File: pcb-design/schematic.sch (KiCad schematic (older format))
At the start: 10 parts, among them J1 TempGauge, J2 FuelGauge, J3 SpeedInput_C2_P10-13, Q3 Q_NPN_BCE

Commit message: Schematic updates, learning KiCad a bit.
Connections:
- net labels added: FuelOutput, SpeedometerOutput, TemperatureOutput
- wire segments 6 -> 0
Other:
- moved on the sheet: J1, J2, J3, Q3, Q?, R1, R2, R3
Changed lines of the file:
@@
 L Device:Q_NPN_BCE Q?
 U 1 1 5D493CD9
-P 3600 5950
-F 0 "Q?" H 3791 5996 50  0000 L CNN
-F 1 "Q_NPN_BCE" H 3791 5905 50  0000 L CNN
-F 2 "" H 3800 6050 50  0001 C CNN
-F 3 "~" H 3600 5950 50  0001 C CNN
-	1    3600 5950
+P 9600 2700
+F 0 "Q?" H 9791 2746 50  0000 L CNN
+F 1 "Q_NPN_BCE" H 9791 2655 50  0000 L CNN
+F 2 "" H 9800 2800 50  0001 C CNN
+F 3 "~" H 9600 2700 50  0001 C CNN
+	1    9600 2700
 	1    0    0    -1
 $EndComp
@@
 L Device:R_Small_US R2
 U 1 1 5D49723D
-P 3300 5950
-F 0 "R2" V 3095 5950 50  0000 C CNN
-F 1 "220" V 3186 5950 50  0000 C CNN
-F 2 "" H 3300 5950 50  0001 C CNN
-F 3 "~" H 3300 5950 50  0001 C CNN
-	1    3300 5950
+P 9300 2700
+F 0 "R2" V 9095 2700 50  0000 C CNN
+F 1 "220" V 9186 2700 50  0000 C CNN
+F 2 "" H 9300 2700 50  0001 C CNN
+F 3 "~" H 9300 2700 50  0001 C CNN
+	1    9300 2700
 	0    1    1    0
 $EndComp
-Wire Wire Line
-	3050 3300 3200 3300
 $Comp
 L Device:Q_NPN_BCE Q?
 U 1 1 5D49F77C
-P 3600 5150
-F 0 "Q?" H 3791 5196 50  0000 L CNN
-F 1 "Q_NPN_BCE" H 3791 5105 50  0000 L CNN
-F 2 "" H 3800 5250 50  0001 C CNN
-F 3 "~" H 3600 5150 50  0001 C CNN
-	1    3600 5150
+P 9600 1800
+F 0 "Q?" H 9791 1846 50  0000 L CNN
+F 1 "Q_NPN_BCE" H 9791 1755 50  0000 L CNN
+F 2 "" H 9800 1900 50  0001 C CNN
+F 3 "~" H 9600 1800 50  0001 C CNN
+	1    9600 1800
 	1    0    0    -1
 $EndComp
@@
 L Device:R_Small_US R1
 U 1 1 5D49F782
-P 3300 5150
-F 0 "R1" V 3095 5150 50  0000 C CNN
-F 1 "470" V 3186 5150 50  0000 C CNN
-F 2 "" H 3300 5150 50  0001 C CNN
-F 3 "~" H 3300 5150 50  0001 C CNN
-	1    3300 5150
+P 9300 1800
+F 0 "R1" V 9095 1800 50  0000 C CNN
+F 1 "470" V 9186 1800 50  0000 C CNN
+F 2 "" H 9300 1800 50  0001 C CNN
+F 3 "~" H 9300 1800 50  0001 C CNN
+	1    9300 1800
 	0    1    1    0
 $EndComp
-Wire Wire Line
-	3200 5150 3200 3300
-Wire Wire Line
-	3200 5950 3150 5950
-Wire Wire Line
-	3150 3400 3050 3400
 $Comp
 L Connector:Conn_01x01_Male J1
 U 1 1 5D4A2526
-P 3900 4950
-F 0 "J1" H 3872 4882 50  0000 R CNN
-F 1 "TempGauge" H 3872 4973 50  0000 R CNN
-F 2 "" H 3900 4950 50  0001 C CNN
-F 3 "~" H 3900 4950 50  0001 C CNN
-	1    3900 4950
+P 9900 1600
+F 0 "J1" H 9872 1532 50  0000 R CNN
+F 1 "TempGauge" H 9872 1623 50  0000 R CNN
+F 2 "" H 9900 1600 50  0001 C CNN
+F 3 "~" H 9900 1600 50  0001 C CNN
+	1    9900 1600
 	-1   0    0    1
 $EndComp
@@
 L Connector:Conn_01x01_Male J2
 U 1 1 5D4A3714
-P 3900 5750
-F 0 "J2" H 3872 5682 50  0000 R CNN
-F 1 "FuelGauge" H 3872 5773 50  0000 R CNN
-F 2 "" H 3900 5750 50  0001 C CNN
-F 3 "~" H 3900 5750 50  0001 C CNN
-	1    3900 5750
+P 9900 2500
+F 0 "J2" H 9872 2432 50  0000 R CNN
+F 1 "FuelGauge" H 9872 2523 50  0000 R CNN
+F 2 "" H 9900 2500 50  0001 C CNN
+F 3 "~" H 9900 2500 50  0001 C CNN
+	1    9900 2500
 	-1   0    0    1
 $EndComp
@@
 L power:GND #PWR?
 U 1 1 5D4A41B3
-P 3700 5350
-F 0 "#PWR?" H 3700 5100 50  0001 C CNN
-F 1 "GND" H 3705 5177 50  0000 C CNN
-F 2 "" H 3700 5350 50  0001 C CNN
-F 3 "" H 3700 5350 50  0001 C CNN
-	1    3700 5350
+P 9700 2000
+F 0 "#PWR?" H 9700 1750 50  0001 C CNN
+F 1 "GND" H 9705 1827 50  0000 C CNN
+F 2 "" H 9700 2000 50  0001 C CNN
+F 3 "" H 9700 2000 50  0001 C CNN
+	1    9700 2000
 	1    0    0    -1
 $EndComp
@@
 L power:GND #PWR?
 U 1 1 5D4A53EC
-P 3700 6150
-F 0 "#PWR?" H 3700 5900 50  0001 C CNN
-F 1 "GND" H 3705 5977 50  0000 C CNN
-F 2 "" H 3700 6150 50  0001 C CNN
-F 3 "" H 3700 6150 50  0001 C CNN
-	1    3700 6150
+P 9700 2900
+F 0 "#PWR?" H 9700 2650 50  0001 C CNN
+F 1 "GND" H 9705 2727 50  0000 C CNN
+F 2 "" H 9700 2900 50  0001 C CNN
+F 3 "" H 9700 2900 50  0001 C CNN
+	1    9700 2900
 	1    0    0    -1
 $EndComp
-Wire Wire Line
-	3150 3400 3150 5950
 $Comp
 L Device:Q_NPN_BCE Q3
 U 1 1 5DD62680
-P 5800 3200
-F 0 "Q3" H 5991 3246 50  0000 L CNN
-F 1 "Q_NPN_BCE" H 5991 3155 50  0000 L CNN
-F 2 "" H 6000 3300 50  0001 C CNN
-F 3 "~" H 5800 3200 50  0001 C CNN
-	1    5800 3200
+P 9600 1050
+F 0 "Q3" H 9791 1096 50  0000 L CNN
+F 1 "Q_NPN_BCE" H 9791 1005 50  0000 L CNN
+F 2 "" H 9800 1150 50  0001 C CNN
+F 3 "~" H 9600 1050 50  0001 C CNN
+	1    9600 1050
 	1    0    0    -1
 $EndComp
@@
 L Device:R_Small_US R3
 U 1 1 5DD62687
-P 5500 3200
-F 0 "R3" V 5295 3200 50  0000 C CNN
-F 1 "470" V 5386 3200 50  0000 C CNN
-F 2 "" H 5500 3200 50  0001 C CNN
-F 3 "~" H 5500 3200 50  0001 C CNN
-	1    5500 3200
+P 9300 1050
+F 0 "R3" V 9095 1050 50  0000 C CNN
+F 1 "470" V 9186 1050 50  0000 C CNN
+F 2 "" H 9300 1050 50  0001 C CNN
+F 3 "~" H 9300 1050 50  0001 C CNN
+	1    9300 1050
 	0    1    1    0
 $EndComp
@@
 L Connector:Conn_01x01_Male J3
 U 1 1 5DD6268E
-P 6100 3000
-F 0 "J3" H 6072 2932 50  0000 R CNN
-F 1 "SpeedInput_C2_P10-13" H 6072 3023 50  0000 R CNN
-F 2 "" H 6100 3000 50  0001 C CNN
-F 3 "~" H 6100 3000 50  0001 C CNN
-	1    6100 3000
+P 9900 850
+F 0 "J3" H 9872 782 50  0000 R CNN
+F 1 "SpeedInput_C2_P10-13" H 9872 873 50  0000 R CNN
+F 2 "" H 9900 850 50  0001 C CNN
+F 3 "~" H 9900 850 50  0001 C CNN
+	1    9900 850
 	-1   0    0    1
 $EndComp
@@
 L power:GND #PWR?
 U 1 1 5DD62695
-P 5900 3400
-F 0 "#PWR?" H 5900 3150 50  0001 C CNN
-F 1 "GND" H 5905 3227 50  0000 C CNN
-F 2 "" H 5900 3400 50  0001 C CNN
-F 3 "" H 5900 3400 50  0001 C CNN
-	1    5900 3400
+P 9700 1250
+F 0 "#PWR?" H 9700 1000 50  0001 C CNN
+F 1 "GND" H 9705 1077 50  0000 C CNN
+F 2 "" H 9700 1250 50  0001 C CNN
+F 3 "" H 9700 1250 50  0001 C CNN
+	1    9700 1250
 	1    0    0    -1
 $EndComp
-Wire Wire Line
-	3050 3200 5400 3200
+Text GLabel 9200 1050 0    50   Input ~ 0
+SpeedometerOutput
+Text GLabel 9200 1800 0    50   Input ~ 0
+TemperatureOutput
+Text GLabel 9200 2700 0    50   Input ~ 0
+FuelOutput
 $EndSCHEMATC

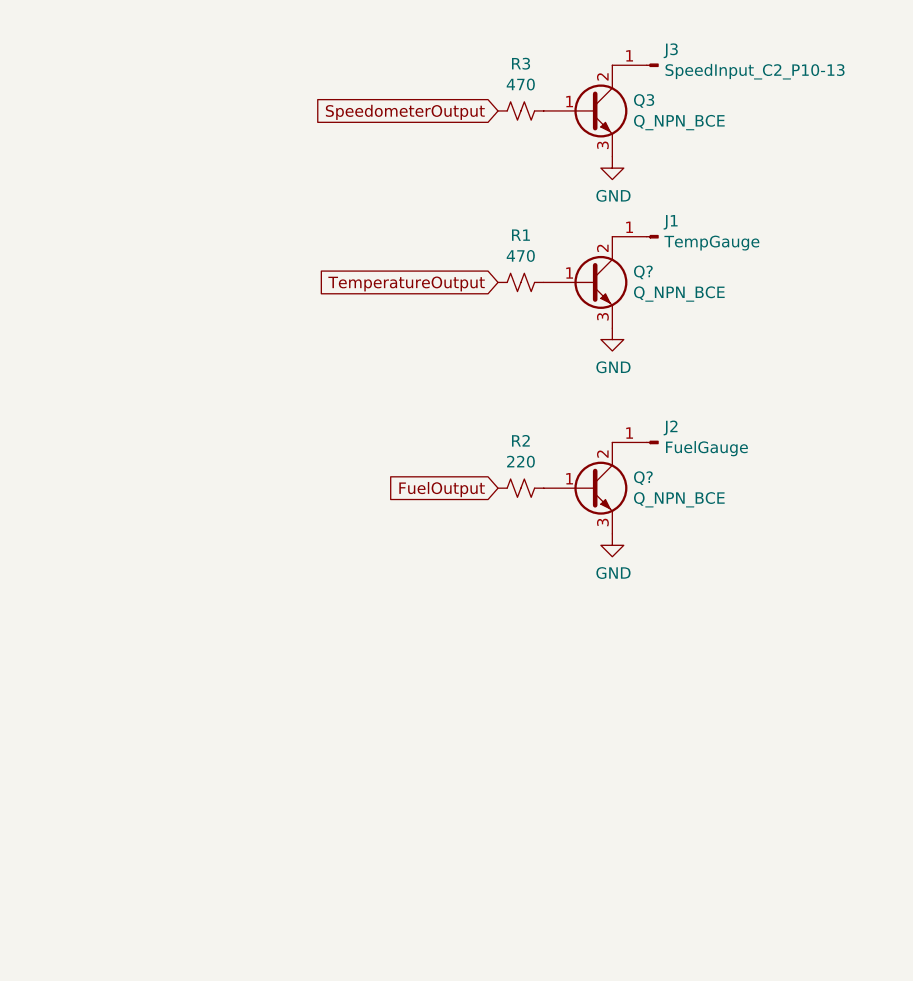
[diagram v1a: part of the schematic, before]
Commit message: Added Tachometer circuit to schematic
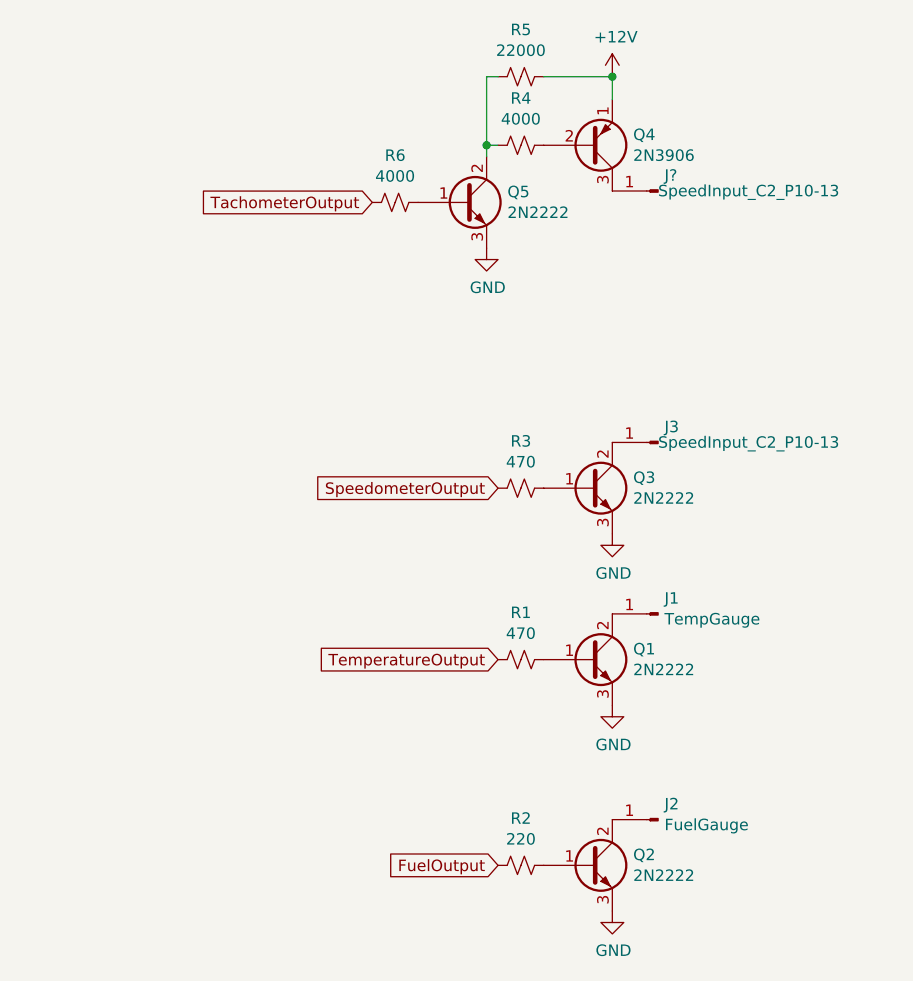
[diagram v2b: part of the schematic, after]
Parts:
- added J?: SpeedInput_C2_P10-13, symbol Connector:Conn_01x01_Male
- added Q4: 2N3906, Package_TO_SOT_THT:TO-92_Inline, symbol Transistor_BJT:2N3906
- added Q5: 2N2222, symbol Device:Q_NPN_BCE
- added R4, R6: 4000, symbol Device:R_Small_US
- added R5: 22000, symbol Device:R_Small_US
- Q1, Q2: renamed from Q?; value Q_NPN_BCE -> 2N2222
- Q3: value Q_NPN_BCE -> 2N2222
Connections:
- net labels added: +12V, TachometerOutput
- wire segments 0 -> 6
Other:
- moved on the sheet: J1, J2, J3, Q1, Q2, Q3, R1, R2, R3
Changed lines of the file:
@@
 $EndComp
 $Comp
-L Device:Q_NPN_BCE Q?
+L Device:Q_NPN_BCE Q2
 U 1 1 5D493CD9
+P 9600 4350
+F 0 "Q2" H 9791 4396 50  0000 L CNN
+F 1 "2N2222" H 9791 4305 50  0000 L CNN
+F 2 "" H 9800 4450 50  0001 C CNN
+F 3 "~" H 9600 4350 50  0001 C CNN
+	1    9600 4350
+	1    0    0    -1
+$EndComp
+$Comp
+L Device:R_Small_US R2
+U 1 1 5D49723D
+P 9300 4350
+F 0 "R2" V 9095 4350 50  0000 C CNN
+F 1 "220" V 9186 4350 50  0000 C CNN
+F 2 "" H 9300 4350 50  0001 C CNN
+F 3 "~" H 9300 4350 50  0001 C CNN
+	1    9300 4350
+	0    1    1    0
+$EndComp
+$Comp
+L Device:Q_NPN_BCE Q1
+U 1 1 5D49F77C
+P 9600 3450
+F 0 "Q1" H 9791 3496 50  0000 L CNN
+F 1 "2N2222" H 9791 3405 50  0000 L CNN
+F 2 "" H 9800 3550 50  0001 C CNN
+F 3 "~" H 9600 3450 50  0001 C CNN
+	1    9600 3450
+	1    0    0    -1
+$EndComp
+$Comp
+L Device:R_Small_US R1
+U 1 1 5D49F782
+P 9300 3450
+F 0 "R1" V 9095 3450 50  0000 C CNN
+F 1 "470" V 9186 3450 50  0000 C CNN
+F 2 "" H 9300 3450 50  0001 C CNN
+F 3 "~" H 9300 3450 50  0001 C CNN
+	1    9300 3450
+	0    1    1    0
+$EndComp
+$Comp
+L Connector:Conn_01x01_Male J1
+U 1 1 5D4A2526
+P 9900 3250
+F 0 "J1" H 9872 3182 50  0000 R CNN
+F 1 "TempGauge" H 9872 3273 50  0000 R CNN
+F 2 "" H 9900 3250 50  0001 C CNN
+F 3 "~" H 9900 3250 50  0001 C CNN
+	1    9900 3250
+	-1   0    0    1
+$EndComp
+$Comp
+L Connector:Conn_01x01_Male J2
+U 1 1 5D4A3714
+P 9900 4150
+F 0 "J2" H 9872 4082 50  0000 R CNN
+F 1 "FuelGauge" H 9872 4173 50  0000 R CNN
+F 2 "" H 9900 4150 50  0001 C CNN
+F 3 "~" H 9900 4150 50  0001 C CNN
+	1    9900 4150
+	-1   0    0    1
+$EndComp
+$Comp
+L power:GND #PWR?
+U 1 1 5D4A41B3
+P 9700 3650
+F 0 "#PWR?" H 9700 3400 50  0001 C CNN
+F 1 "GND" H 9705 3477 50  0000 C CNN
+F 2 "" H 9700 3650 50  0001 C CNN
+F 3 "" H 9700 3650 50  0001 C CNN
+	1    9700 3650
+	1    0    0    -1
+$EndComp
+$Comp
+L power:GND #PWR?
+U 1 1 5D4A53EC
+P 9700 4550
+F 0 "#PWR?" H 9700 4300 50  0001 C CNN
+F 1 "GND" H 9705 4377 50  0000 C CNN
+F 2 "" H 9700 4550 50  0001 C CNN
+F 3 "" H 9700 4550 50  0001 C CNN
+	1    9700 4550
+	1    0    0    -1
+$EndComp
+$Comp
+L Device:Q_NPN_BCE Q3
+U 1 1 5DD62680
 P 9600 2700
-F 0 "Q?" H 9791 2746 50  0000 L CNN
-F 1 "Q_NPN_BCE" H 9791 2655 50  0000 L CNN
+F 0 "Q3" H 9791 2746 50  0000 L CNN
+F 1 "2N2222" H 9791 2655 50  0000 L CNN
 F 2 "" H 9800 2800 50  0001 C CNN
 F 3 "~" H 9600 2700 50  0001 C CNN
@@
 $EndComp
 $Comp
-L Device:R_Small_US R2
-U 1 1 5D49723D
+L Device:R_Small_US R3
+U 1 1 5DD62687
 P 9300 2700
-F 0 "R2" V 9095 2700 50  0000 C CNN
-F 1 "220" V 9186 2700 50  0000 C CNN
+F 0 "R3" V 9095 2700 50  0000 C CNN
+F 1 "470" V 9186 2700 50  0000 C CNN
 F 2 "" H 9300 2700 50  0001 C CNN
 F 3 "~" H 9300 2700 50  0001 C CNN
@@
 $EndComp
 $Comp
-L Device:Q_NPN_BCE Q?
-U 1 1 5D49F77C
-P 9600 1800
-F 0 "Q?" H 9791 1846 50  0000 L CNN
-F 1 "Q_NPN_BCE" H 9791 1755 50  0000 L CNN
-F 2 "" H 9800 1900 50  0001 C CNN
-F 3 "~" H 9600 1800 50  0001 C CNN
-	1    9600 1800
-	1    0    0    -1
-$EndComp
-$Comp
-L Device:R_Small_US R1
-U 1 1 5D49F782
-P 9300 1800
-F 0 "R1" V 9095 1800 50  0000 C CNN
-F 1 "470" V 9186 1800 50  0000 C CNN
-F 2 "" H 9300 1800 50  0001 C CNN
-F 3 "~" H 9300 1800 50  0001 C CNN
-	1    9300 1800
-	0    1    1    0
-$EndComp
-$Comp
-L Connector:Conn_01x01_Male J1
-U 1 1 5D4A2526
-P 9900 1600
-F 0 "J1" H 9872 1532 50  0000 R CNN
-F 1 "TempGauge" H 9872 1623 50  0000 R CNN
-F 2 "" H 9900 1600 50  0001 C CNN
-F 3 "~" H 9900 1600 50  0001 C CNN
-	1    9900 1600
-	-1   0    0    1
-$EndComp
-$Comp
-L Connector:Conn_01x01_Male J2
-U 1 1 5D4A3714
+L Connector:Conn_01x01_Male J3
+U 1 1 5DD6268E
 P 9900 2500
-F 0 "J2" H 9872 2432 50  0000 R CNN
-F 1 "FuelGauge" H 9872 2523 50  0000 R CNN
+F 0 "J3" H 9872 2432 50  0000 R CNN
+F 1 "SpeedInput_C2_P10-13" H 9900 2500 50  0000 R CNN
 F 2 "" H 9900 2500 50  0001 C CNN
 F 3 "~" H 9900 2500 50  0001 C CNN
@@
 $Comp
 L power:GND #PWR?
-U 1 1 5D4A41B3
-P 9700 2000
-F 0 "#PWR?" H 9700 1750 50  0001 C CNN
-F 1 "GND" H 9705 1827 50  0000 C CNN
-F 2 "" H 9700 2000 50  0001 C CNN
-F 3 "" H 9700 2000 50  0001 C CNN
-	1    9700 2000
-	1    0    0    -1
-$EndComp
-$Comp
-L power:GND #PWR?
-U 1 1 5D4A53EC
+U 1 1 5DD62695
 P 9700 2900
 F 0 "#PWR?" H 9700 2650 50  0001 C CNN
@@
 	1    0    0    -1
 $EndComp
-$Comp
-L Device:Q_NPN_BCE Q3
-U 1 1 5DD62680
-P 9600 1050
-F 0 "Q3" H 9791 1096 50  0000 L CNN
-F 1 "Q_NPN_BCE" H 9791 1005 50  0000 L CNN
-F 2 "" H 9800 1150 50  0001 C CNN
-F 3 "~" H 9600 1050 50  0001 C CNN
-	1    9600 1050
-	1    0    0    -1
-$EndComp
-$Comp
-L Device:R_Small_US R3
-U 1 1 5DD62687
-P 9300 1050
-F 0 "R3" V 9095 1050 50  0000 C CNN
-F 1 "470" V 9186 1050 50  0000 C CNN
-F 2 "" H 9300 1050 50  0001 C CNN
-F 3 "~" H 9300 1050 50  0001 C CNN
-	1    9300 1050
-	0    1    1    0
-$EndComp
-$Comp
-L Connector:Conn_01x01_Male J3
-U 1 1 5DD6268E
-P 9900 850
-F 0 "J3" H 9872 782 50  0000 R CNN
-F 1 "SpeedInput_C2_P10-13" H 9872 873 50  0000 R CNN
-F 2 "" H 9900 850 50  0001 C CNN
-F 3 "~" H 9900 850 50  0001 C CNN
-	1    9900 850
-	-1   0    0    1
-$EndComp
-$Comp
-L power:GND #PWR?
-U 1 1 5DD62695
-P 9700 1250
-F 0 "#PWR?" H 9700 1000 50  0001 C CNN
-F 1 "GND" H 9705 1077 50  0000 C CNN
-F 2 "" H 9700 1250 50  0001 C CNN
-F 3 "" H 9700 1250 50  0001 C CNN
-	1    9700 1250
-	1    0    0    -1
-$EndComp
-Text GLabel 9200 1050 0    50   Input ~ 0
+Text GLabel 9200 2700 0    50   Input ~ 0
 SpeedometerOutput
-Text GLabel 9200 1800 0    50   Input ~ 0
+Text GLabel 9200 3450 0    50   Input ~ 0
 TemperatureOutput
-Text GLabel 9200 2700 0    50   Input ~ 0
+Text GLabel 9200 4350 0    50   Input ~ 0
 FuelOutput
+$Comp
+L Transistor_BJT:2N3906 Q4
+U 1 1 5DDF4E90
+P 9600 1200
+F 0 "Q4" H 9791 1154 50  0000 L CNN
+F 1 "2N3906" H 9791 1245 50  0000 L CNN
+F 2 "Package_TO_SOT_THT:TO-92_Inline" H 9800 1125 50  0001 L CIN
+F 3 "https://www.fairchildsemi.com/datasheets/2N/2N3906.pdf" H 9600 1200 50  0001 L CNN
+	1    9600 1200
+	1    0    0    1
+$EndComp
+$Comp
+L Device:R_Small_US R4
+U 1 1 5DDF52DA
+P 9300 1200
+F 0 "R4" V 9095 1200 50  0000 C CNN
+F 1 "4000" V 9186 1200 50  0000 C CNN
+F 2 "" H 9300 1200 50  0001 C CNN
+F 3 "~" H 9300 1200 50  0001 C CNN
+	1    9300 1200
+	0    1    1    0
+$EndComp
+$Comp
+L Device:R_Small_US R5
+U 1 1 5DDF54A7
+P 9300 900
+F 0 "R5" V 9095 900 50  0000 C CNN
+F 1 "22000" V 9186 900 50  0000 C CNN
+F 2 "" H 9300 900 50  0001 C CNN
+F 3 "~" H 9300 900 50  0001 C CNN
+	1    9300 900
+	0    1    1    0
+$EndComp
+Wire Wire Line
+	9200 1200 9150 1200
+Wire Wire Line
+	9150 1200 9150 1250
+Wire Wire Line
+	9700 1000 9700 900
+Wire Wire Line
+	9700 900  9400 900
+Wire Wire Line
+	9200 900  9150 900
+Wire Wire Line
+	9150 900  9150 1200
+Connection ~ 9150 1200
+$Comp
+L Device:R_Small_US R6
+U 1 1 5DDF56FD
+P 8750 1450
+F 0 "R6" V 8545 1450 50  0000 C CNN
+F 1 "4000" V 8636 1450 50  0000 C CNN
+F 2 "" H 8750 1450 50  0001 C CNN
+F 3 "~" H 8750 1450 50  0001 C CNN
+	1    8750 1450
+	0    1    1    0
+$EndComp
+$Comp
+L power:GND #PWR?
+U 1 1 5DDF5843
+P 9150 1650
+F 0 "#PWR?" H 9150 1400 50  0001 C CNN
+F 1 "GND" H 9155 1477 50  0000 C CNN
+F 2 "" H 9150 1650 50  0001 C CNN
+F 3 "" H 9150 1650 50  0001 C CNN
+	1    9150 1650
+	1    0    0    -1
+$EndComp
+$Comp
+L power:+12V #PWR?
+U 1 1 5DDF5F07
+P 9700 900
+F 0 "#PWR?" H 9700 750 50  0001 C CNN
+F 1 "+12V" H 9715 1073 50  0000 C CNN
+F 2 "" H 9700 900 50  0001 C CNN
+F 3 "" H 9700 900 50  0001 C CNN
+	1    9700 900
+	1    0    0    -1
+$EndComp
+Connection ~ 9700 900
+Text GLabel 8650 1450 0    50   Input ~ 0
+TachometerOutput
+$Comp
+L Connector:Conn_01x01_Male J?
+U 1 1 5DDF676D
+P 9900 1400
+F 0 "J?" H 9872 1332 50  0000 R CNN
+F 1 "SpeedInput_C2_P10-13" H 9900 1400 50  0000 R CNN
+F 2 "" H 9900 1400 50  0001 C CNN
+F 3 "~" H 9900 1400 50  0001 C CNN
+	1    9900 1400
+	-1   0    0    1
+$EndComp
+$Comp
+L Device:Q_NPN_BCE Q5
+U 1 1 5DDF6B21
+P 9050 1450
+F 0 "Q5" H 9241 1496 50  0000 L CNN
+F 1 "2N2222" H 9241 1405 50  0000 L CNN
+F 2 "" H 9250 1550 50  0001 C CNN
+F 3 "~" H 9050 1450 50  0001 C CNN
+	1    9050 1450
+	1    0    0    -1
+$EndComp
 $EndSCHEMATC

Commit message: Don't track the workspace file and don't track .sch-bak data.
Created a schematic for the indicator lights circuit.
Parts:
- removed J?: SpeedInput_C2_P10-13, symbol Connector:Conn_01x01_Male
- removed Q4: 2N3906, Package_TO_SOT_THT:TO-92_Inline, symbol Transistor_BJT:2N3906
- removed Q5: 2N2222, symbol Device:Q_NPN_BCE
- removed R4, R6: 4000, symbol Device:R_Small_US
- removed R5: 22000, symbol Device:R_Small_US
- added J5, J6: SpeedInput_C2_P10-13, TestPoint:TestPoint_Pad_D2.5mm, symbol Connector:Conn_01x01_Male
- added Q6, Q7: 2N2222, Package_TO_SOT_THT:TO-92_HandSolder, symbol Device:Q_NPN_BCE
- added Q8, Q9: 2N3906, Package_TO_SOT_THT:TO-92_Inline, symbol Transistor_BJT:2N3906
- added R10, R12, R7, R8: 4000, Resistor_SMD:R_1206_3216Metric_Pad1.42x1.75mm_HandSolder, symbol Device:R_Small_US
- added R11, R9: 22000, Resistor_SMD:R_1206_3216Metric_Pad1.42x1.75mm_HandSolder, symbol Device:R_Small_US
- J1, J2, J3: footprint (none) -> TestPoint:TestPoint_Pad_D2.5mm
- Q1, Q2, Q3: footprint (none) -> Package_TO_SOT_THT:TO-92_HandSolder
- R1, R2, R3: footprint (none) -> Resistor_SMD:R_1206_3216Metric_Pad1.42x1.75mm_HandSolder
- gave numbers to parts that had none: 1
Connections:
- wire segments 6 -> 27

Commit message: Checking in schematic files
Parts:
- added J4: Screw_Terminal_01x02, symbol Connector:Screw_Terminal_01x02
- added U3: MCP2562-E-P, Package_DIP:DIP-8_W7.62mm, symbol Interface_CAN_LIN:MCP2562-E-P
- U1: symbol RF_Module:ESP32-WROOM-32 -> schematic-rescue:ESP32-WROOM-32-RF_Module
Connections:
- net labels added: +3V3, +5V, ESP_CAN0_RX, ESP_CAN0_TX
- wire segments 27 -> 31
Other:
- note added: "CANBus Transciever"
- note added: "Tachometer Output \nDarlington Transistor - +12v"
- moved on the sheet: J5, Q6, Q8, R10, R7, R9
